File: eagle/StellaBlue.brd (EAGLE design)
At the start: 108.9 x 85.8 mm, 89 parts, among them IC1 74LS245N, IC2 74LS245N, IC3 74LS245N, IC5 7805TV, T1 2N3906, T2 2N3904, T3 2N3906, T4 2N3904, X1 FMS6141

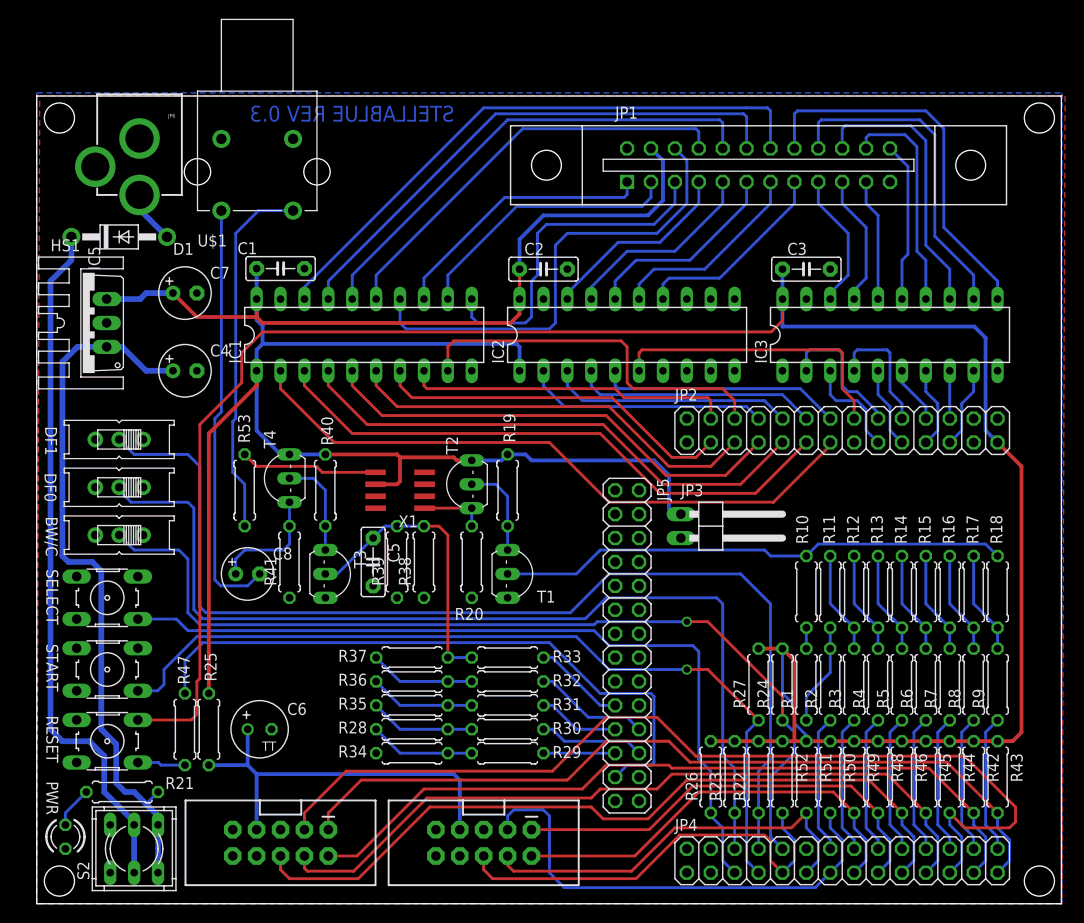
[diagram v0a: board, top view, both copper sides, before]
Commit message: labels replacement
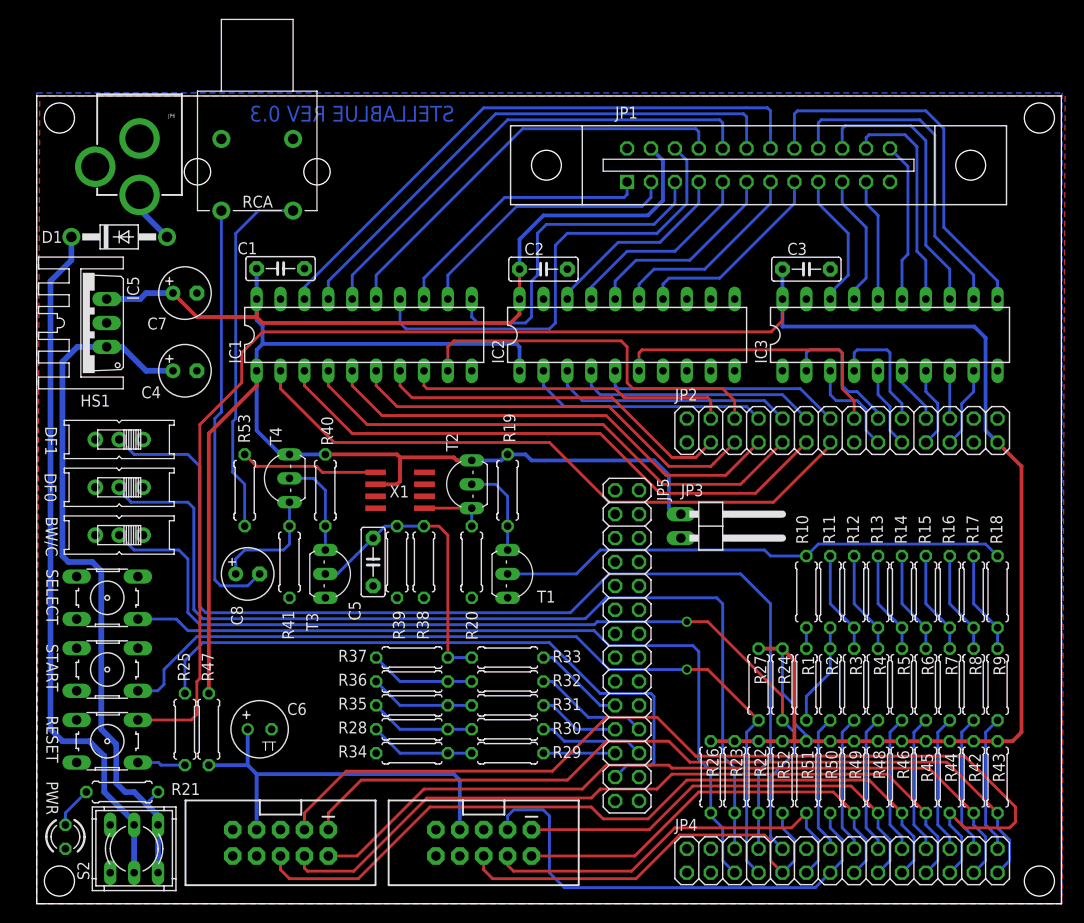
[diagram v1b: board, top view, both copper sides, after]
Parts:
- JP1: value (none) -> CARTRIDGE
- renumbered U$1 to RCA

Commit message: labels positioning
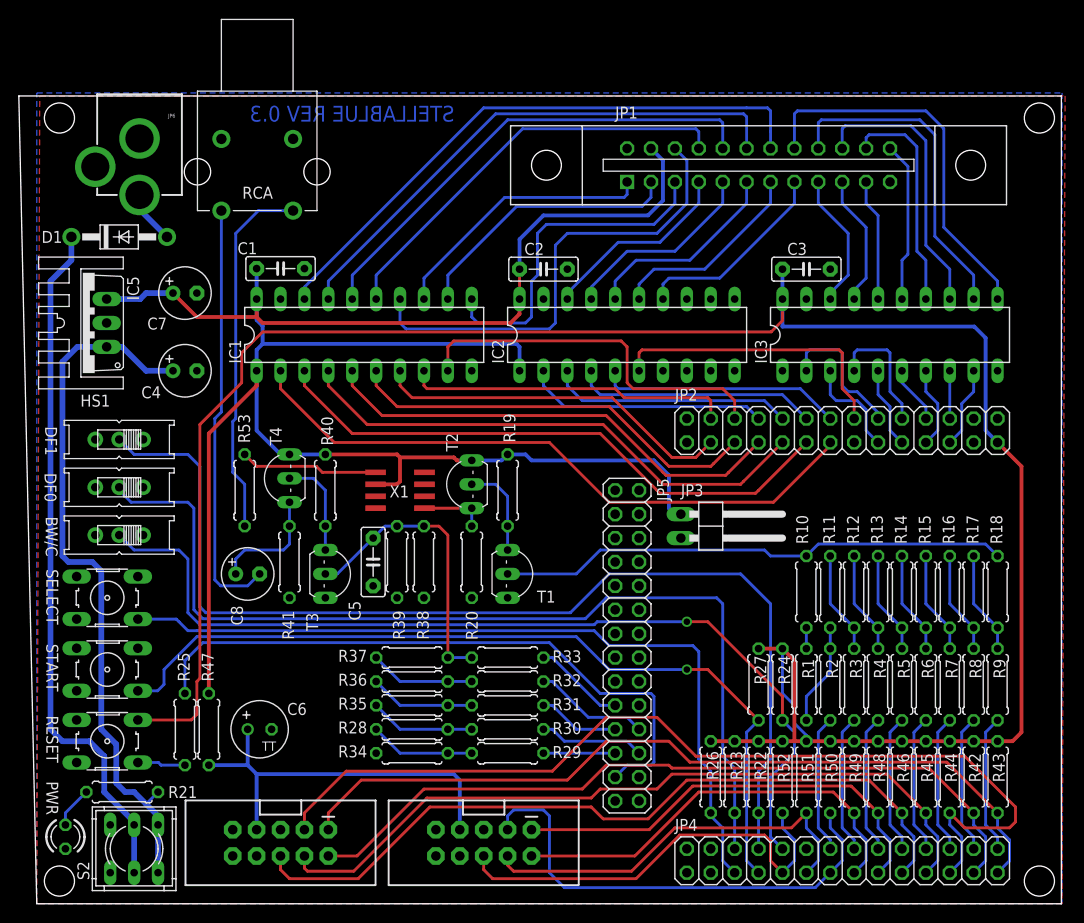
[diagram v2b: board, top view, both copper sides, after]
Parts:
- JP1: value CARTRIDGE -> CARTRIDGE SOCKET
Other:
- board size 108.9 x 85.8 mm -> 110.8 x 85.8 mm

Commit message: Corrected board dimentions
Daniel favor verificar
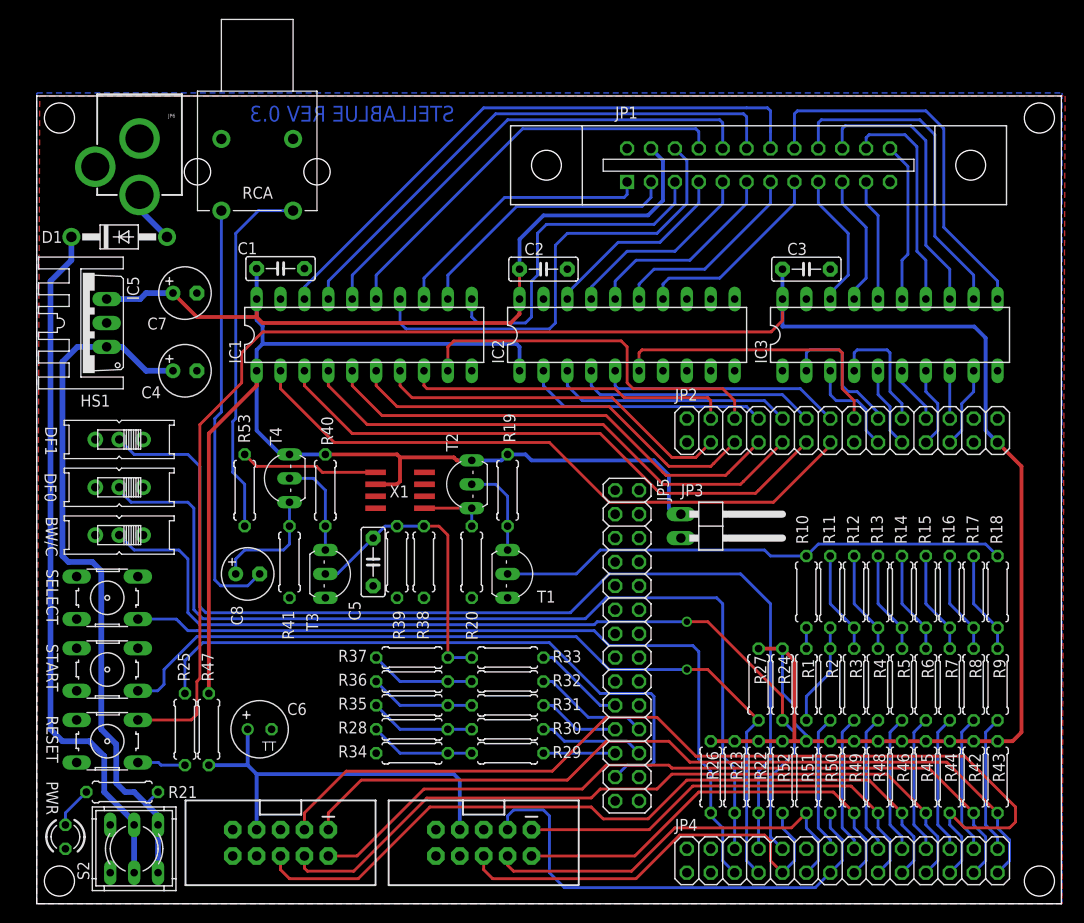
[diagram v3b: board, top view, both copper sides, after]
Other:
- board size 110.8 x 85.8 mm -> 108.9 x 85.8 mm
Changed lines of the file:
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@@
 <grid distance="0.0125" unitdist="inch" unit="inch" style="lines" multiple="8" display="yes" altdistance="0.00625" altunitdist="inch" altunit="inch"/>
 <layers>
-<layer number="1" name="Top" color="4" fill="1" visible="no" active="yes"/>
+<layer number="1" name="Top" color="4" fill="1" visible="yes" active="yes"/>
 <layer number="2" name="Route2" color="1" fill="3" visible="no" active="no"/>
 <layer number="3" name="Route3" color="4" fill="3" visible="no" active="no"/>
@@
 <layer number="14" name="Route14" color="1" fill="6" visible="no" active="no"/>
 <layer number="15" name="Route15" color="4" fill="6" visible="no" active="no"/>
-<layer number="16" name="Bottom" color="1" fill="1" visible="no" active="yes"/>
+<layer number="16" name="Bottom" color="1" fill="1" visible="yes" active="yes"/>
 <layer number="17" name="Pads" color="2" fill="1" visible="yes" active="yes"/>
 <layer number="18" name="Vias" color="2" fill="1" visible="yes" active="yes"/>
@@
 <wire x1="-0.508" y1="-0.762" x2="108.382" y2="-0.762" width="0" layer="20"/>
 <wire x1="108.382" y1="-0.762" x2="108.382" y2="85.08" width="0" layer="20"/>
-<wire x1="108.382" y1="85.08" x2="-2.413" y2="85.08" width="0" layer="20"/>
-<wire x1="-2.413" y1="85.08" x2="-0.508" y2="-0.762" width="0" layer="20"/>
+<wire x1="108.382" y1="85.08" x2="-0.508" y2="85.08" width="0" layer="20"/>
+<wire x1="-0.508" y1="85.08" x2="-0.508" y2="-0.762" width="0" layer="20"/>
 <hole x="1.905" y="82.7405" drill="3.2"/>
 <hole x="1.905" y="1.651" drill="3.2"/>
